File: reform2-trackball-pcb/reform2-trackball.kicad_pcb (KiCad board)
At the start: 2 copper layers, 83.4 x 59 mm, 42 parts, among them J1 Conn_USB, J2 Conn_01x06_Female, SW1 Choc, SW2 Choc, SW3 Choc, SW4 Choc, SW5 Choc, SW6 SW_RST, SW7 SW_HWB, U1 ATmega32U2-AU, U2 TLV75533PDBV, Y1 Crystal_GND24

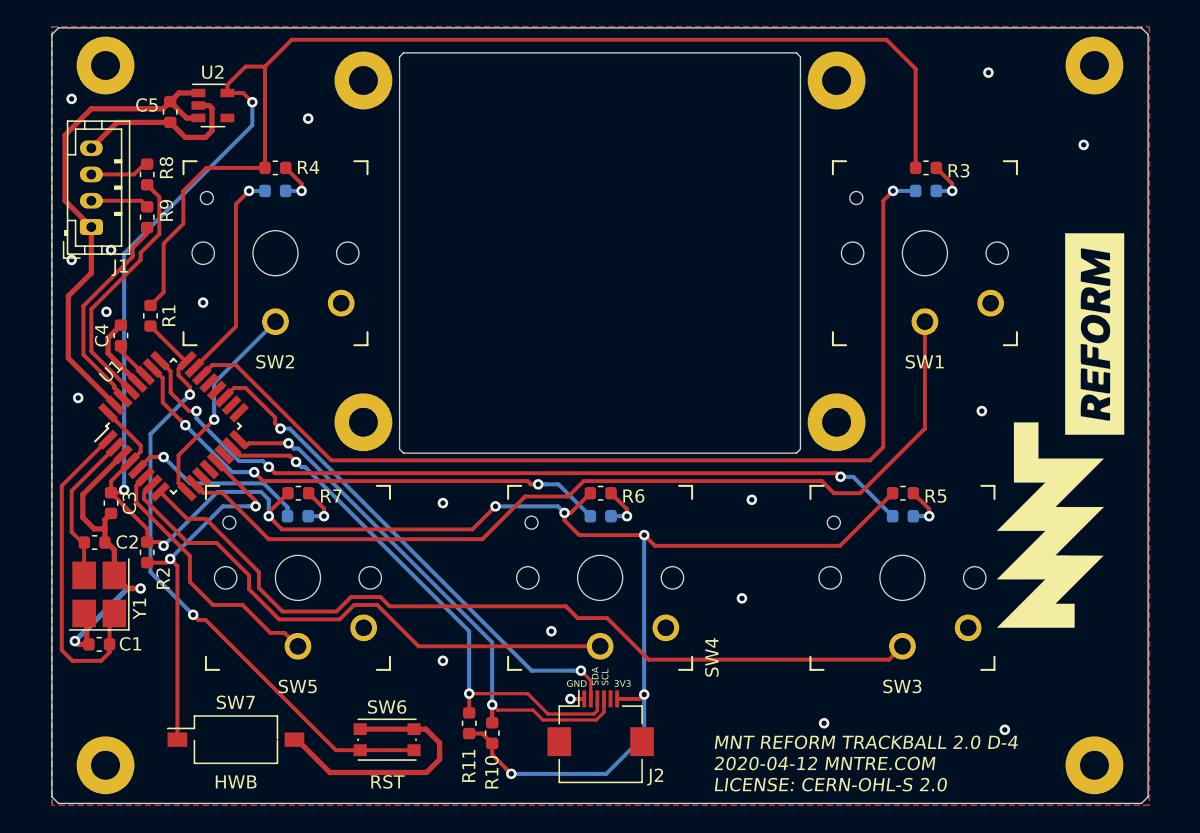
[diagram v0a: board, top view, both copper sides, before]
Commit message: trackball-pcb: R-1 version with ESD protection and fuse
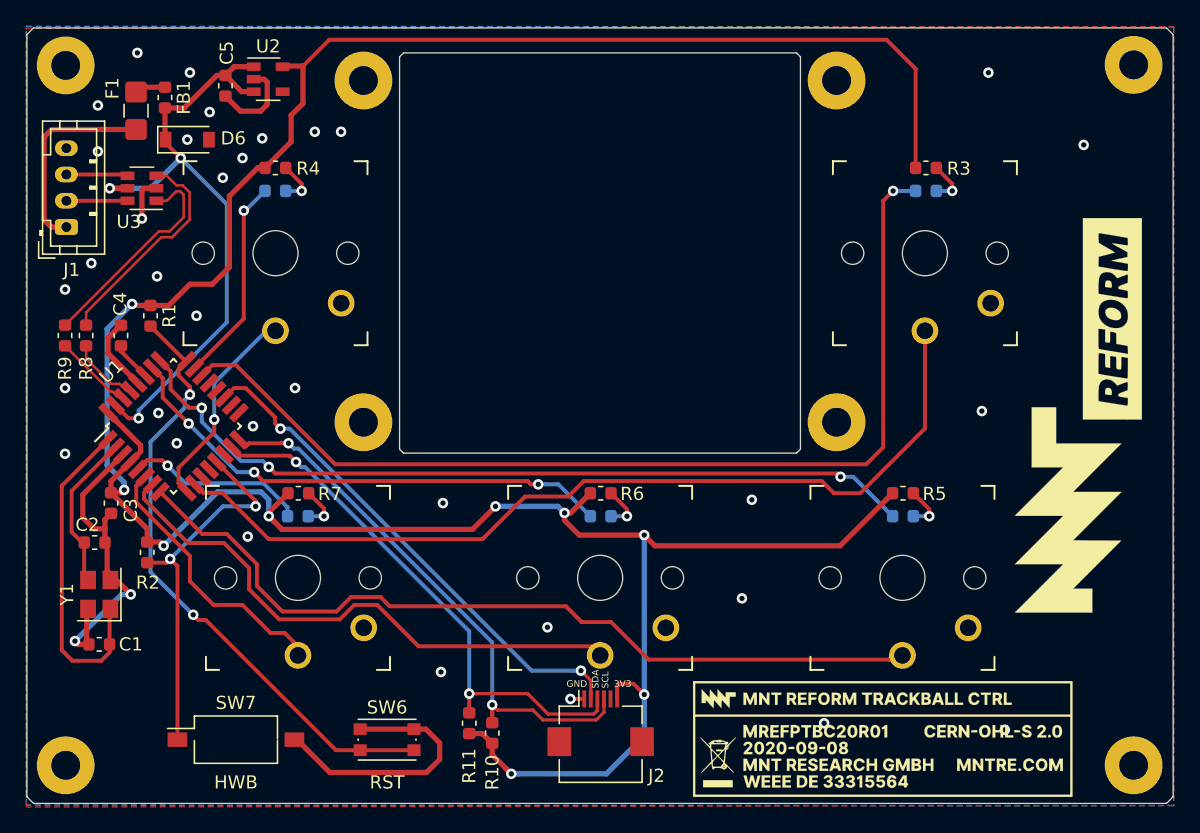
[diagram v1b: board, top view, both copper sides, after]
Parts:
- added D6: BZT52-B5V6J, Diode_SMD:D_SOD-123, F.Cu at (119.3, 58.6)
- added F1: 0ZCJ0075AF2E, Fuse:Fuse_1206_3216Metric_Castellated, F.Cu at (115.4, 56.4)
- added FB1: BLM18PG221SH1D, Inductor_SMD:L_0603_1608Metric, F.Cu at (117.6, 55.4)
- added MK1: BADGE, footprints-trackball:mntreform-trackball-badge, F.Cu at (172.2, 104.2)
- added U3: USBLC6-2SC6, Package_TO_SOT_SMD:SOT-23-6, F.Cu at (115.8, 62.3)
- Y1: footprint Crystals:Crystal_SMD_3225-4pin_3.2x2.5mm_HandSoldering -> Crystal:Crystal_SMD_3225-4Pin_3.2x2.5mm
- moved R8 13.1 mm to (111.6, 73.5)
- moved R9 11.0 mm to (110.0, 73.5)
- moved C5 4.65 mm to (122.2, 54.5)
- moved U2 4.65 mm to (125.5, 54.0)
- moved MK5 3.03 mm to (110.0, 53.0)
- moved MK8 3.03 mm to (110.0, 106.2)
- moved MK6 2.98 mm to (191.3, 53.0)
- moved MK7 2.98 mm to (191.3, 106.2)
- moved J1 1.90 mm to (110.1, 65.2)
- moved MK13 1.77 mm to (187.1, 79.6)
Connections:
- net Net-(R8-Pad2) renamed /D+
- net Net-(R9-Pad1) renamed /D-
- J1 pad 1: +5V -> /5V_IN
- J1 pad 2: Net-(J1-Pad2) -> /PD-
- J1 pad 3: Net-(J1-Pad3) -> /PD+
- R8 pad 1: Net-(J1-Pad3) -> /UD+
- R9 pad 2: Net-(J1-Pad2) -> /UD-
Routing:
- net +3V3: track 240.5 -> 217.8 mm
- net /UD+: track 0.00 -> 16.9 mm
- net /UD-: track 0.00 -> 16.6 mm
- net /5V_IN: track 0.00 -> 15.5 mm
- net /D+: track 19.4 -> 5.33 mm
- net +5V: track 37.7 -> 48.9 mm, vias 0 -> 3
- net /D-: track 16.2 -> 6.03 mm
- net GND: track 66.4 -> 61.5 mm, vias 20 -> 36
- net /PD+: track 0.00 -> 4.69 mm
- net /PD-: track 0.00 -> 4.65 mm
- net Net-(J1-Pad3): track 4.58 -> 0.00 mm
- net Net-(J1-Pad2): track 4.44 -> 0.00 mm
- net Net-(F1-Pad1): track 0.00 -> 2.35 mm
- net Net-(D2-Pad1): track 16.4 -> 15.8 mm
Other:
- board size 83.4 x 59 mm -> 87.2 x 59 mm
- board text removed: "MNT REFORM TRACKBALL 2.0 D-4 2020-04-12 MNTRE.COM LICENSE: CERN-OHL-S 2.0"
